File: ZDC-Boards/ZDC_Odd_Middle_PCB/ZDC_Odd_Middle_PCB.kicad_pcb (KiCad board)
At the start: 2 copper layers, 195.2 x 643 mm, 95 parts

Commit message: Added new stencil
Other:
- board text removed: "10 nF"
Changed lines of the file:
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@@
 			(layer "F.Fab")
 		)
-		(fp_text user "${REFERENCE}"
-			(at 0 -2.4 0)
-			(layer "F.Fab")
-			(effects
-				(font
-					(size 0.8 0.8)
-					(thickness 0.12)
-				)
-			)
-		)
 		(pad "1" smd roundrect
 			(at -1.475 0)
@@
 			(layer "F.Fab")
 		)
-		(fp_text user "${REFERENCE}"
-			(at 0 -2.4 0)
-			(layer "F.Fab")
-			(effects
-				(font
-					(size 0.8 0.8)
-					(thickness 0.12)
-				)
-			)
-		)
 		(pad "1" smd roundrect
 			(at -1.475 0)
@@
 			)
 		)
-	)
-	(gr_text "10 nF"
-		(at 169.6 -626 0)
-		(layer "F.Fab")
-		(effects
-			(font
-				(size 0.8 0.8)
-				(thickness 0.12)
-			)
-		)
-	)
-	(gr_text "10 nF"
-		(at 72 -626 0)
-		(layer "F.Fab")
-		(effects
-			(font
-				(size 0.8 0.8)
-				(thickness 0.12)
-			)
-		)

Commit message: Updated ZDC connectors to pad connections, v2.0
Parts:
- removed REF** (x2): PinHeader_2x25_P1.27mm_Horizontal, Connector_PinHeader_1.27mm:PinHeader_2x25_P1.27mm_Horizontal
- added J1: TE_5-104895-5_AMPMODU_50-50_2x25_P1.27mm_Horizontal_SMD, TE_AMPMODU:TE_5-104895-5_AMPMODU_50-50_2x25_P1.27mm_Horizontal_SMD, F.Cu at (48.8, -634.4)
- added J2: TE_5-104895-5_AMPMODU_50-50_2x25_P1.27mm_Horizontal_SMD, TE_AMPMODU:TE_5-104895-5_AMPMODU_50-50_2x25_P1.27mm_Horizontal_SMD, F.Cu at (146.4, -634.4)
- #MK1, #MK2: renamed from REF**20; footprint SiPM:S14160-1315PS_dimple_silkscreen_with_capacitor -> SiPM:S14160-1315PS_silkscreen_marker
- C0, C1, C10, C11, C12, C13, C14, C15, C16, C17, C18, C19, C2, C20, C21, C22, C23, C24, C25, C26, C27, C28, C29, C3, C30, C31, C32, C33, C34, C35, C36, C37, C38, C39, C4, C40, C41, C42, C43, C5, C6, C7, C8, C9: renamed from 10 nF
- J3: renamed from REF**; footprint Connector_Coaxial:BNC_TEConnectivity_1478035_Horizontal -> ZDC:BNC_TEConnectivity_1478035_Horizontal_EdgePads
- renumbered REF**20 to D0, REF**20 to D1, REF**20 to D10, REF**20 to D11, REF**20 to D12, REF**20 to D13, REF**20 to D14, REF**20 to D15, REF**20 to D16, REF**20 to D17, REF**20 to D18, REF**20 to D19, REF**20 to D2, REF**20 to D20, REF**20 to D21, REF**20 to D22, REF**20 to D23, REF**20 to D24, REF**20 to D25, REF**20 to D26, REF**20 to D27, REF**20 to D28, REF**20 to D29, REF**20 to D3, REF**20 to D30, REF**20 to D31, REF**20 to D32, REF**20 to D33, REF**20 to D34, REF**20 to D35, REF**20 to D36, REF**20 to D37, REF**20 to D38, REF**20 to D39, REF**20 to D4, REF**20 to D40, REF**20 to D41, REF**20 to D42, REF**20 to D43, REF**20 to D5, REF**20 to D6, REF**20 to D7, REF**20 to D8, REF**20 to D9, REF** to J4
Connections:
- C11 pad 1: K12 -> K11
- C12 pad 1: K13 -> K12
- C13 pad 1: K14 -> K13
- C14 pad 1: K15 -> K14
- C15 pad 1: K16 -> K15
- C16 pad 1: K17 -> K16
- C17 pad 1: K18 -> K17
- C18 pad 1: K19 -> K18
- C19 pad 1: K20 -> K19
- C20 pad 1: K21 -> K20
- C21 pad 1: K22 -> K21
- C22 pad 1: K0 -> K22
- C23 pad 1: K1 -> K23
- C24 pad 1: K2 -> K24
- C25 pad 1: K3 -> K25
- C26 pad 1: K4 -> K26
- C27 pad 1: K5 -> K27
- C28 pad 1: K6 -> K28
- C29 pad 1: K7 -> K29
- C30 pad 1: K8 -> K30
- C31 pad 1: K9 -> K31
- C32 pad 1: K10 -> K32
- C33 pad 1: K12 -> K33
- C34 pad 1: K13 -> K34
- C35 pad 1: K14 -> K35
- C36 pad 1: K15 -> K36
- C37 pad 1: K16 -> K37
- C38 pad 1: K17 -> K38
- C39 pad 1: K18 -> K39
- C40 pad 1: K19 -> K40
- C41 pad 1: K20 -> K41
- C42 pad 1: K21 -> K42
- C43 pad 1: K22 -> K43
- D0 pad : LK -> LK1
- D0 pad 7: (no net) -> K0
- D0 pad 8: (no net) -> A0
- D0 pad 9: LA -> LA1
- D1 pad : LK -> LK1
- D1 pad 7: (no net) -> K1
- D1 pad 8: (no net) -> A1
- D1 pad 9: LA -> LA1
- D10 pad : LK -> LK1
- D10 pad 7: (no net) -> K10
- D10 pad 8: (no net) -> A10
- D10 pad 9: LA -> LA1
- D11 pad : LK -> LK1
- D11 pad 7: K12 -> K11
- D11 pad 8: A12 -> A11
- D11 pad 9: LA -> LA1
- D12 pad : LK -> LK1
- D12 pad 7: (no net) -> K12
- D12 pad 8: (no net) -> A12
- D12 pad 9: LA -> LA1
- D13 pad : LK -> LK1
- D13 pad 7: (no net) -> K13
- D13 pad 8: (no net) -> A13
- D13 pad 9: LA -> LA1
- D14 pad : LK -> LK1
- D14 pad 7: (no net) -> K14
- D14 pad 8: (no net) -> A14
- D14 pad 9: LA -> LA1
- D15 pad : LK -> LK1
- D15 pad 7: (no net) -> K15
- D15 pad 8: (no net) -> A15
- D15 pad 9: LA -> LA1
- D16 pad : LK -> LK1
- D16 pad 7: (no net) -> K16
- D16 pad 8: A17 -> A16
- D16 pad 9: LA -> LA1
- D17 pad : LK -> LK1
- D17 pad 7: (no net) -> K17
- D17 pad 8: (no net) -> A17
- D17 pad 9: LA -> LA1
- D18 pad : LK -> LK1
- D18 pad 7: (no net) -> K18
- D18 pad 8: (no net) -> A18
- D18 pad 9: LA -> LA1
- D19 pad : LK -> LK1
- D19 pad 7: (no net) -> K19
- D19 pad 8: (no net) -> A19
- D19 pad 9: LA -> LA1
- D2 pad : LK -> LK1
- D2 pad 7: (no net) -> K2
- D2 pad 8: (no net) -> A2
- D2 pad 9: LA -> LA1
- D20 pad : LK -> LK1
- D20 pad 7: (no net) -> K20
- D20 pad 8: (no net) -> A20
- D20 pad 9: LA -> LA1
- D21 pad : LK -> LK1
- D21 pad 7: (no net) -> K21
- D21 pad 8: (no net) -> A21
- D21 pad 9: LA -> LA1
- D22 pad : LK -> LK2
- D22 pad 7: (no net) -> K22
- D22 pad 8: (no net) -> A22
- D22 pad 9: LA -> LA2
- D23 pad : LK -> LK2
- D23 pad 7: (no net) -> K23
- D23 pad 8: (no net) -> A23
- D23 pad 9: LA -> LA2
- D24 pad : LK -> LK2
- D24 pad 7: (no net) -> K24
- D24 pad 8: (no net) -> A24
- D24 pad 9: LA -> LA2
- D25 pad : LK -> LK2
- D25 pad 7: (no net) -> K25
- D25 pad 8: (no net) -> A25
- D25 pad 9: LA -> LA2
- D26 pad : LK -> LK2
- D26 pad 7: (no net) -> K26
- D26 pad 8: (no net) -> A26
- D26 pad 9: LA -> LA2
- D27 pad : LK -> LK2
- D27 pad 7: (no net) -> K27
- D27 pad 8: A5 -> A27
- D27 pad 9: LA -> LA2
- D28 pad : LK -> LK2
- D28 pad 7: (no net) -> K28
- D28 pad 8: (no net) -> A28
- D28 pad 9: LA -> LA2
- D29 pad : LK -> LK2
- D29 pad 7: (no net) -> K29
- D29 pad 8: (no net) -> A29
- D29 pad 9: LA -> LA2
- D3 pad : LK -> LK1
- D3 pad 7: (no net) -> K3
- D3 pad 8: (no net) -> A3
- D3 pad 9: LA -> LA1
- D30 pad : LK -> LK2
- D30 pad 7: (no net) -> K30
- D30 pad 8: (no net) -> A30
- D30 pad 9: LA -> LA2
- D31 pad : LK -> LK2
- D31 pad 7: (no net) -> K31
- D31 pad 8: (no net) -> A31
- D31 pad 9: LA -> LA2
- D32 pad : LK -> LK2
- D32 pad 7: (no net) -> K32
- D32 pad 8: (no net) -> A32
- D32 pad 9: LA -> LA2
- D33 pad : LK -> LK2
- D33 pad 7: K12 -> K33
- D33 pad 8: A12 -> A33
- D33 pad 9: LA -> LA2
- D34 pad : LK -> LK2
- D34 pad 7: (no net) -> K34
- D34 pad 8: (no net) -> A34
- D34 pad 9: LA -> LA2
- D35 pad : LK -> LK2
- D35 pad 7: (no net) -> K35
- D35 pad 8: (no net) -> A35
- D35 pad 9: LA -> LA2
- D36 pad : LK -> LK2
- D36 pad 7: (no net) -> K36
- D36 pad 8: (no net) -> A36
- D36 pad 9: LA -> LA2
- D37 pad : LK -> LK2
- D37 pad 7: (no net) -> K37
- D37 pad 8: (no net) -> A37
- D37 pad 9: LA -> LA2
- D38 pad : LK -> LK2
- D38 pad 7: (no net) -> K38
- D38 pad 8: A17 -> A38
- D38 pad 9: LA -> LA2
- D39 pad : LK -> LK2
- D39 pad 7: (no net) -> K39
- D39 pad 8: (no net) -> A39
- D39 pad 9: LA -> LA2
- D4 pad : LK -> LK1
- D4 pad 7: (no net) -> K4
- D4 pad 8: (no net) -> A4
- D4 pad 9: LA -> LA1
- D40 pad : LK -> LK2
- D40 pad 7: (no net) -> K40
- D40 pad 8: (no net) -> A40
- D40 pad 9: LA -> LA2
- D41 pad : LK -> LK2
- D41 pad 7: (no net) -> K41
- D41 pad 8: (no net) -> A41
- D41 pad 9: LA -> LA2
- D42 pad : LK -> LK2
- D42 pad 7: (no net) -> K42
- D42 pad 8: (no net) -> A42
- D42 pad 9: LA -> LA2
- D43 pad : LK -> LK2
- D43 pad 7: (no net) -> K43
- D43 pad 8: (no net) -> A43
- D43 pad 9: LA -> LA2
- D5 pad : LK -> LK1
- D5 pad 7: (no net) -> K5
- D5 pad 9: LA -> LA1
- D6 pad : LK -> LK1
- D6 pad 7: (no net) -> K6
- D6 pad 8: (no net) -> A6
- D6 pad 9: LA -> LA1
- D7 pad : LK -> LK1
- D7 pad 7: (no net) -> K7
- D7 pad 8: (no net) -> A7
- D7 pad 9: LA -> LA1
- D8 pad : LK -> LK1
- D8 pad 7: (no net) -> K8
- D8 pad 8: (no net) -> A8
- D8 pad 9: LA -> LA1
- D9 pad : LK -> LK1
- D9 pad 7: (no net) -> K9
- D9 pad 8: (no net) -> A9
- D9 pad 9: LA -> LA1
- J3 pad 1: LA -> LA1
- J3 pad 2: LK -> LK1
- J4 pad 1: LA -> LA2
- J4 pad 2: LK -> LK2
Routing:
- net LK: track 2379.6 -> 0.00 mm, vias 44 -> 0
- net LA: track 2279.3 -> 0.00 mm, vias 2 -> 0
- net LK2: track 0.00 -> 1189.8 mm, vias 0 -> 22
- net LK1: track 0.00 -> 1189.8 mm, vias 0 -> 22
- net A22: track 1267.6 -> 117.7 mm
- net LA2: track 0.00 -> 1141.6 mm, vias 0 -> 1
- net LA1: track 0.00 -> 1141.6 mm, vias 0 -> 1
- net K22: track 1235.8 -> 120.5 mm, vias 4 -> 2
- net A43: track 0.00 -> 634.3 mm
- net A32: track 0.00 -> 631.3 mm
- net K43: track 0.00 -> 618.5 mm, vias 0 -> 2
- net A10: track 1242.2 -> 631.3 mm
- net K10: track 1197.8 -> 597.7 mm, vias 4 -> 2
- net K32: track 0.00 -> 597.7 mm, vias 0 -> 2
- net A42: track 0.00 -> 588.9 mm
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- added copper zone on B.Cu, net (none)
- added copper zone on F.Cu, net (none)
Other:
- board text added: "TE 5-104895-5 (AMPMODU 50/50 R/A SMT)"
- board text added: "ZDC Odd Middle PCB v2.0 Designed by Sean Preins"
- board text removed: "PinHeader_2x25_P1.27mm_Horizontal"
- board text removed: "ZDC Odd Middle PCB v1.0 Designed by Sean Preins"

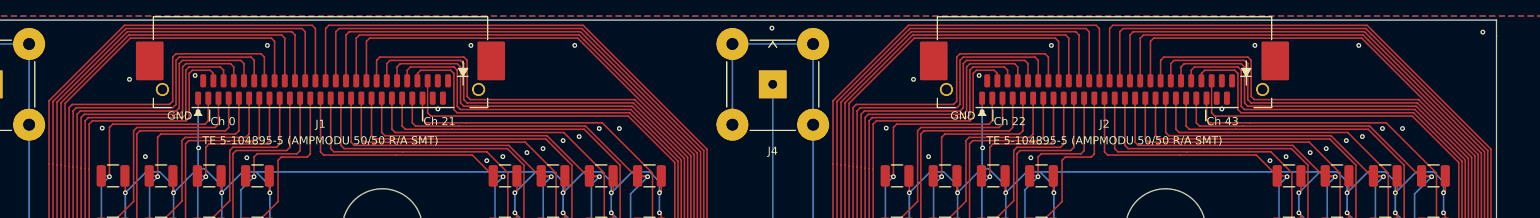
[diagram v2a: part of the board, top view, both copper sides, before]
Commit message: Updated ZDC boards to use new pin connectors that attach to crimped cables
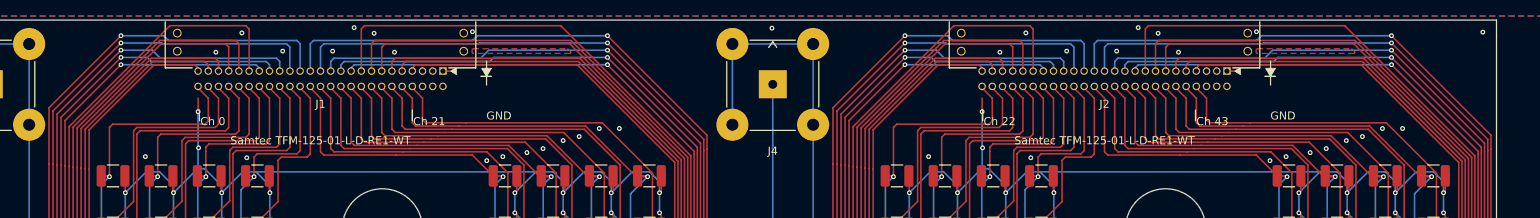
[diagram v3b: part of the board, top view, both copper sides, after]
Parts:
- J1, J2: value TE_5-104895-5_AMPMODU_50-50_2x25_P1.27mm_Horizontal_SMD -> Samtec_TFM-125-01-x-D-RE1-WT_2x25_P1.27mm_Horizontal; footprint TE_AMPMODU:TE_5-104895-5_AMPMODU_50-50_2x25_P1.27mm_Horizontal_SMD -> Samtec_TFM:Samtec_TFM-125-01-x-D-RE1-WT_2x25_P1.27mm_Horizontal
- moved #MK2 3.02 mm to (167.0, -636.0)
- moved #MK1 2.92 mm to (69.4, -636.0)
- moved J1 1.34 mm to (48.8, -635.7), turned to 0 degrees
- moved J2 1.34 mm to (146.4, -635.7), turned to 0 degrees
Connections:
- J1 pad 10: A3 -> K20
- J1 pad 11: K4 -> A19
- J1 pad 12: A4 -> K19
- J1 pad 13: K5 -> A18
- J1 pad 14: A5 -> K18
- J1 pad 15: K6 -> A17
- J1 pad 16: A6 -> K17
- J1 pad 17: K7 -> A16
- J1 pad 18: A7 -> K16
- J1 pad 19: K8 -> A15
- J1 pad 20: A8 -> K15
- J1 pad 21: K9 -> A14
- J1 pad 22: A9 -> K14
- J1 pad 23: K10 -> A13
- J1 pad 24: A10 -> K13
- J1 pad 25: K11 -> A12
- J1 pad 26: A11 -> K12
- J1 pad 27: K12 -> A11
- J1 pad 28: A12 -> K11
- J1 pad 29: K13 -> A10
- J1 pad 3: K0 -> (no net)
- J1 pad 30: A13 -> K10
- J1 pad 31: K14 -> A9
- J1 pad 32: A14 -> K9
- J1 pad 33: K15 -> A8
- J1 pad 34: A15 -> K8
- J1 pad 35: K16 -> A7
- J1 pad 36: A16 -> K7
- J1 pad 37: K17 -> A6
- J1 pad 38: A17 -> K6
- J1 pad 39: K18 -> A5
- J1 pad 4: A0 -> (no net)
- J1 pad 40: A18 -> K5
- J1 pad 41: K19 -> A4
- J1 pad 42: A19 -> K4
- J1 pad 43: K20 -> A3
- J1 pad 44: A20 -> K3
- J1 pad 45: K21 -> A2
- J1 pad 46: A21 -> K2
- J1 pad 47: (no net) -> A1
- J1 pad 48: (no net) -> K1
- J1 pad 49: (no net) -> A0
- J1 pad 5: K1 -> (no net)
- J1 pad 50: (no net) -> K0
- J1 pad 6: A1 -> (no net)
- J1 pad 7: K2 -> A21
- J1 pad 8: A2 -> K21
- J1 pad 9: K3 -> A20
- J1 pad MP: (no net) -> GND
- J2 pad 10: A25 -> K42
- J2 pad 11: K26 -> A41
- J2 pad 12: A26 -> K41
- J2 pad 13: K27 -> A40
- J2 pad 14: A27 -> K40
- J2 pad 15: K28 -> A39
- J2 pad 16: A28 -> K39
- J2 pad 17: K29 -> A38
- J2 pad 18: A29 -> K38
- J2 pad 19: K30 -> A37
- J2 pad 20: A30 -> K37
- J2 pad 21: K31 -> A36
- J2 pad 22: A31 -> K36
- J2 pad 23: K32 -> A35
- J2 pad 24: A32 -> K35
- J2 pad 25: K33 -> A34
- J2 pad 26: A33 -> K34
- J2 pad 27: K34 -> A33
- J2 pad 28: A34 -> K33
- J2 pad 29: K35 -> A32
- J2 pad 3: K22 -> (no net)
- J2 pad 30: A35 -> K32
- J2 pad 31: K36 -> A31
- J2 pad 32: A36 -> K31
- J2 pad 33: K37 -> A30
- J2 pad 34: A37 -> K30
- J2 pad 35: K38 -> A29
- J2 pad 36: A38 -> K29
- J2 pad 37: K39 -> A28
- J2 pad 38: A39 -> K28
- J2 pad 39: K40 -> A27
- J2 pad 4: A22 -> (no net)
- J2 pad 40: A40 -> K27
- J2 pad 41: K41 -> A26
- J2 pad 42: A41 -> K26
- J2 pad 43: K42 -> A25
- J2 pad 44: A42 -> K25
- J2 pad 45: K43 -> A24
- J2 pad 46: A43 -> K24
- J2 pad 47: (no net) -> A23
- J2 pad 48: (no net) -> K23
- J2 pad 49: (no net) -> A22
- J2 pad 5: K23 -> (no net)
- J2 pad 50: (no net) -> K22
- J2 pad 6: A23 -> (no net)
- J2 pad 7: K24 -> A43
- J2 pad 8: A24 -> K43
- J2 pad 9: K25 -> A42
- J2 pad MP: (no net) -> GND
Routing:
- net A28: track 425.7 -> 416.7 mm, vias 0 -> 1
- net A6: track 425.7 -> 416.7 mm, vias 0 -> 1
- net A7: track 477.1 -> 468.7 mm, vias 0 -> 1
- net A29: track 477.1 -> 468.7 mm, vias 0 -> 1
- net A30: track 528.5 -> 520.7 mm, vias 0 -> 1
- net A8: track 528.5 -> 520.7 mm, vias 0 -> 1
- net A9: track 579.9 -> 573.5 mm, vias 0 -> 1
- net A31: track 579.9 -> 573.5 mm, vias 0 -> 1
- net A24: track 220.3 -> 214.1 mm
- net A2: track 220.3 -> 214.1 mm
- net A23: track 168.7 -> 162.7 mm
- net A1: track 168.7 -> 162.7 mm
- net A32: track 631.3 -> 625.5 mm, vias 0 -> 1
- net A10: track 631.3 -> 625.5 mm, vias 0 -> 1
- net A0: track 117.7 -> 112.0 mm
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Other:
- board text added: "Samtec TFM-125-01-L-D-RE1-WT"
- board text removed: "TE 5-104895-5 (AMPMODU 50/50 R/A SMT)"
